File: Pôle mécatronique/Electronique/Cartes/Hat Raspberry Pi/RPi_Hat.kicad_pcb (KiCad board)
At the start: 2 copper layers, 65 x 57.3 mm, 14 parts, among them J1 Conn_02x03_Odd_Even, J2 RPi_GPIO, U1 XBee, U2 MCP25625, Y1 8MHz

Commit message: Update alim correction
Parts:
- added ?: , , F.Cu at (73.4, 67.1)
- added ?: , , F.Cu at (73.4, 62.2)
- added R1: R, Resistor_THT:R_Axial_DIN0207_L6.3mm_D2.5mm_P2.54mm_Vertical, F.Cu at (75.9, 66.5)
- U2: value MCP25625 -> MCP25625-x-SS
- moved R3 22.1 mm to (94.7, 62.0), turned to -90 degrees
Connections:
- J2 pad 39: GND -> unconnected-(J2-Pad39)
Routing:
- net /RPi_GPIO/BCM14_TXD: track 46.4 -> 57.3 mm
- net GND: track 55.7 -> 47.1 mm, vias 6 -> 4
- net 5VRPI: track 79.9 -> 72.4 mm
- net can_L: track 12.3 -> 18.6 mm, vias 2 -> 0
- net 3V3: track 107.8 -> 102.4 mm
- net /RPi_GPIO/BCM15_RXD: track 50.1 -> 53.7 mm
- net cmd_relais: track 33.6 -> 36.6 mm
- net Net-(C3-Pad1): track 22.4 -> 24.5 mm
- net Net-(R3-Pad2): track 7.39 -> 8.38 mm
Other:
- board size 65 x 57.3 mm -> 65 x 58.5 mm

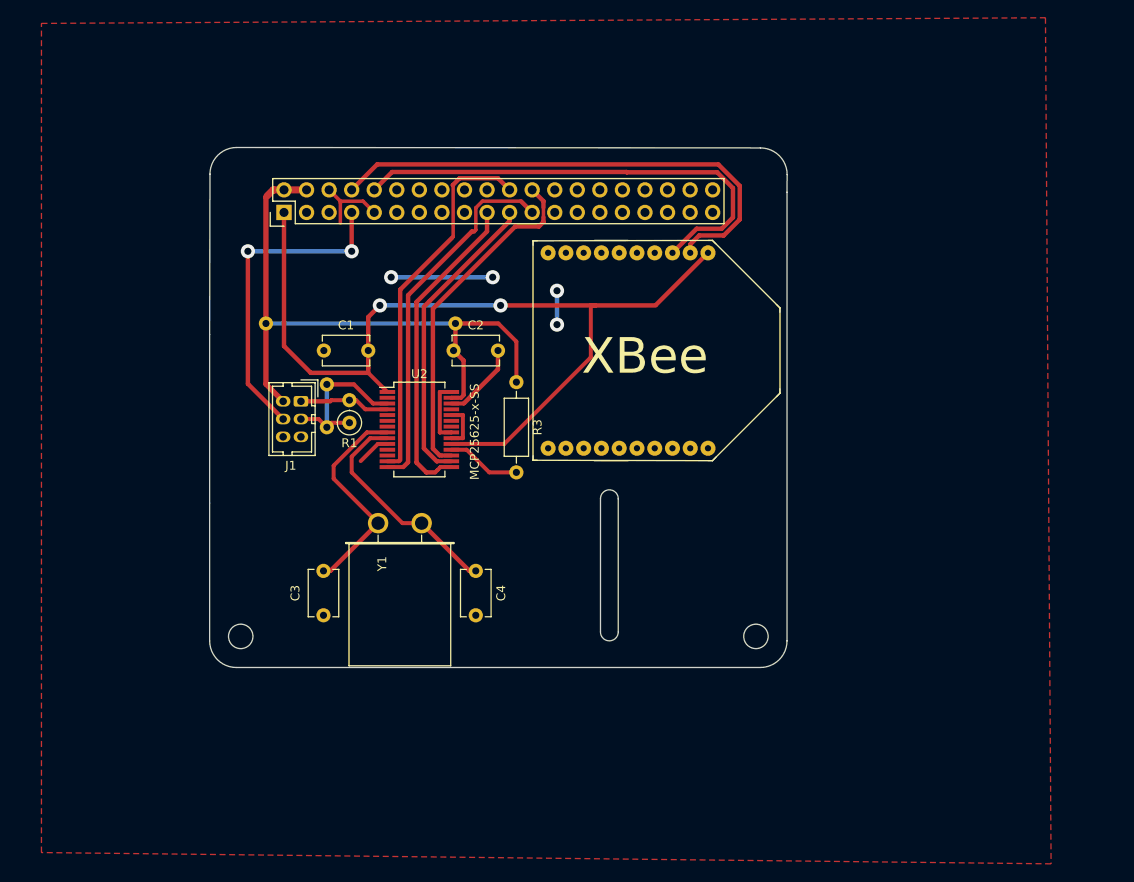
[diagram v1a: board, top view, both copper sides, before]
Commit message: Update HAT
- Ajout des pads
- Correction du schéma
- Corrections diverses
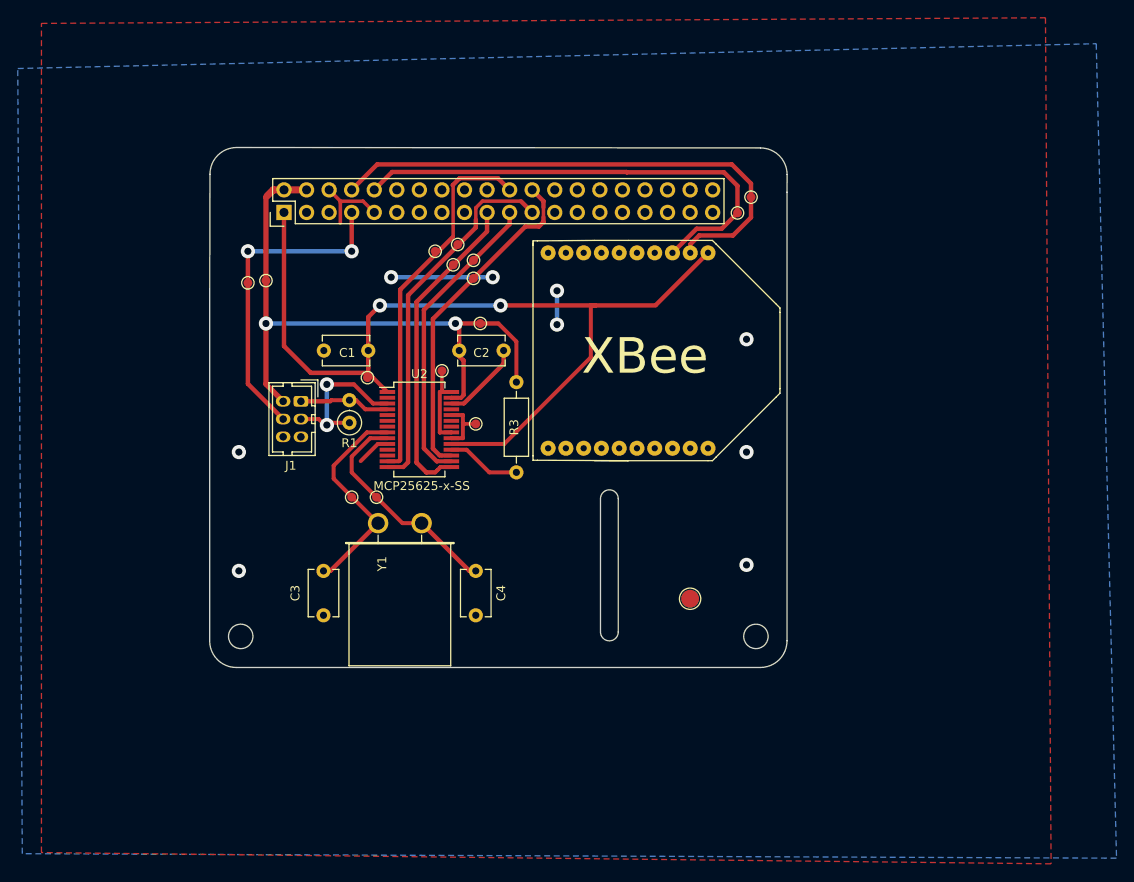
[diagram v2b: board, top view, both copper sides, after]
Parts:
- removed the ? at (73.4, 67.1)
- removed the ? at (66.5, 55.4)
- removed the ? at (73.4, 62.2)
- removed the ? at (87.9, 55.4)
- added  : TestPoint_Pad_D1.0mm, TestPoint:TestPoint_Pad_D1.0mm, F.Cu at (79.0, 74.9)
- added  : TestPoint_Pad_D1.0mm, TestPoint:TestPoint_Pad_D1.0mm, F.Cu at (76.2, 74.9)
- added ?: , , B.Cu at (114.3, 86.4)
- added REF**: TestPoint_Pad_D1.0mm, TestPoint:TestPoint_Pad_D1.0mm, F.Cu at (66.5, 50.5)
- added REF**: TestPoint_Pad_D1.0mm, TestPoint:TestPoint_Pad_D1.0mm, F.Cu at (64.5, 50.8)
- added REF**: TestPoint_Pad_D2.0mm, TestPoint:TestPoint_Pad_D2.0mm, F.Cu at (114.3, 86.4)
- added REF**: TestPoint_Pad_D1.0mm, TestPoint:TestPoint_Pad_D1.0mm, F.Cu at (121.2, 41.1)
- added REF**: TestPoint_Pad_D1.0mm, TestPoint:TestPoint_Pad_D1.0mm, F.Cu at (86.4, 60.7)
- added REF**: TestPoint_Pad_D1.0mm, TestPoint:TestPoint_Pad_D1.0mm, F.Cu at (87.6, 48.8)
- added REF**: TestPoint_Pad_D1.0mm, TestPoint:TestPoint_Pad_D1.0mm, F.Cu at (89.9, 48.3)
- added REF**: TestPoint_Pad_D1.0mm, TestPoint:TestPoint_Pad_D1.0mm, F.Cu at (90.7, 55.4)
- added REF**: TestPoint_Pad_D1.0mm, TestPoint:TestPoint_Pad_D1.0mm, F.Cu at (119.6, 42.9)
- added REF**: TestPoint_Pad_D1.0mm, TestPoint:TestPoint_Pad_D1.0mm, F.Cu at (90.2, 66.7)
- added REF**: TestPoint_Pad_D1.0mm, TestPoint:TestPoint_Pad_D1.0mm, F.Cu at (88.1, 46.5)
- added REF**: TestPoint_Pad_D1.0mm, TestPoint:TestPoint_Pad_D1.0mm, F.Cu at (78.0, 61.5)
- added REF**: TestPoint_Pad_D1.0mm, TestPoint:TestPoint_Pad_D1.0mm, F.Cu at (85.6, 47.2)
- added REF**: TestPoint_Pad_D1.0mm, TestPoint:TestPoint_Pad_D1.0mm, F.Cu at (89.9, 50.3)
- moved C2 0.64 mm to (88.3, 58.4)
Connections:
- net 3V3 renamed +3.3VA
- net 5VRPI renamed +5V
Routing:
- net GND: track 47.1 -> 39.7 mm, vias 4 -> 9
- net /RPi_GPIO/BCM14_TXD: track 57.3 -> 59.9 mm
- net Net-(U2-Pad21): track 7.15 -> 9.36 mm
- net Net-(U2-Pad20): track 5.20 -> 6.72 mm
- net /RPi_GPIO/BCM15_RXD: track 53.7 -> 54.6 mm
- net CS: track 38.8 -> 38.1 mm
- net +5V: track 72.4 -> 72.3 mm, vias 0 -> 2
- net can_L: vias 0 -> 2
- added copper zone on B.Cu, net GND

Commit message: Update
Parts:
- moved J1 2.18 mm to (68.3, 64.0)
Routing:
- net can_H: track 10.2 -> 12.3 mm
- net can_L: track 18.6 -> 20.4 mm
- net +5V: track 72.3 -> 71.4 mm
- net cmd_relais: track 36.6 -> 35.9 mm

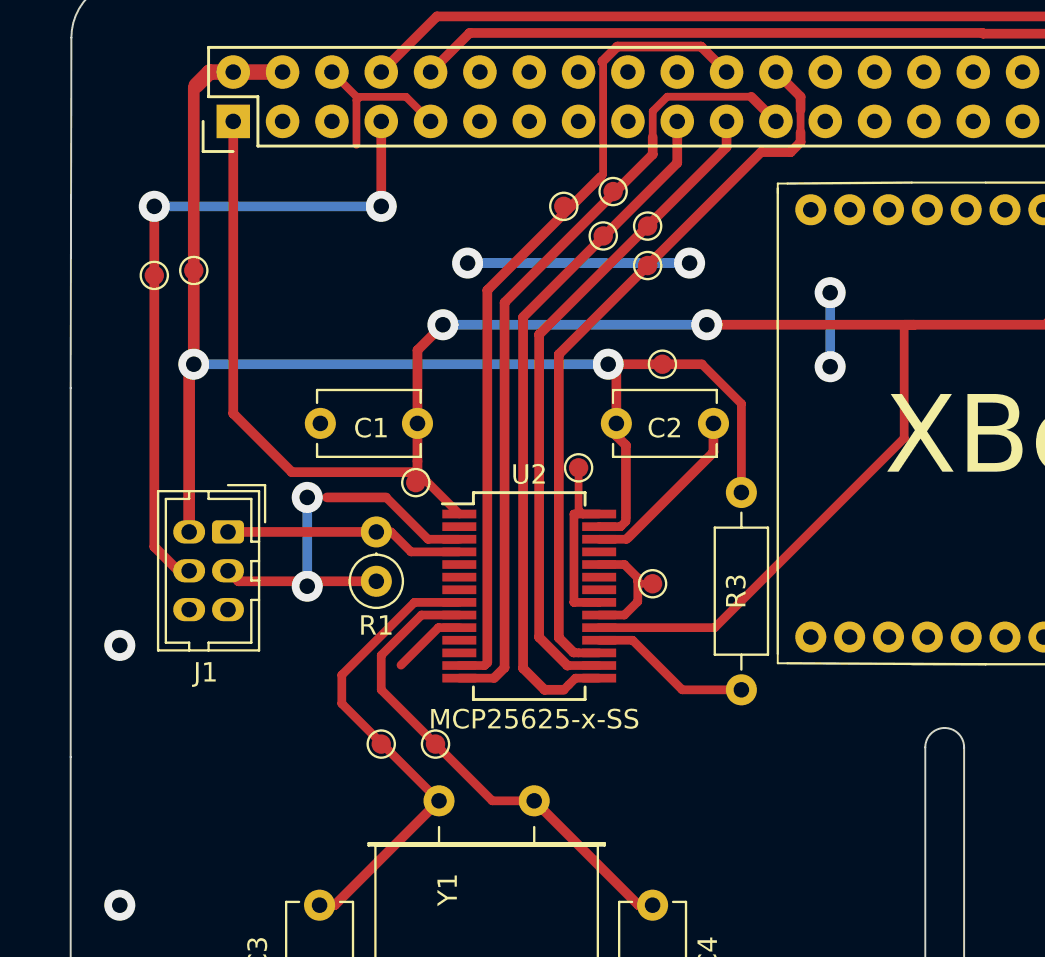
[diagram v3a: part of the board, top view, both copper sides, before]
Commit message: Update HAT & Archi
HAT : - Ajout de l'interrupteur logique de démarrage

Archi : - Update générale
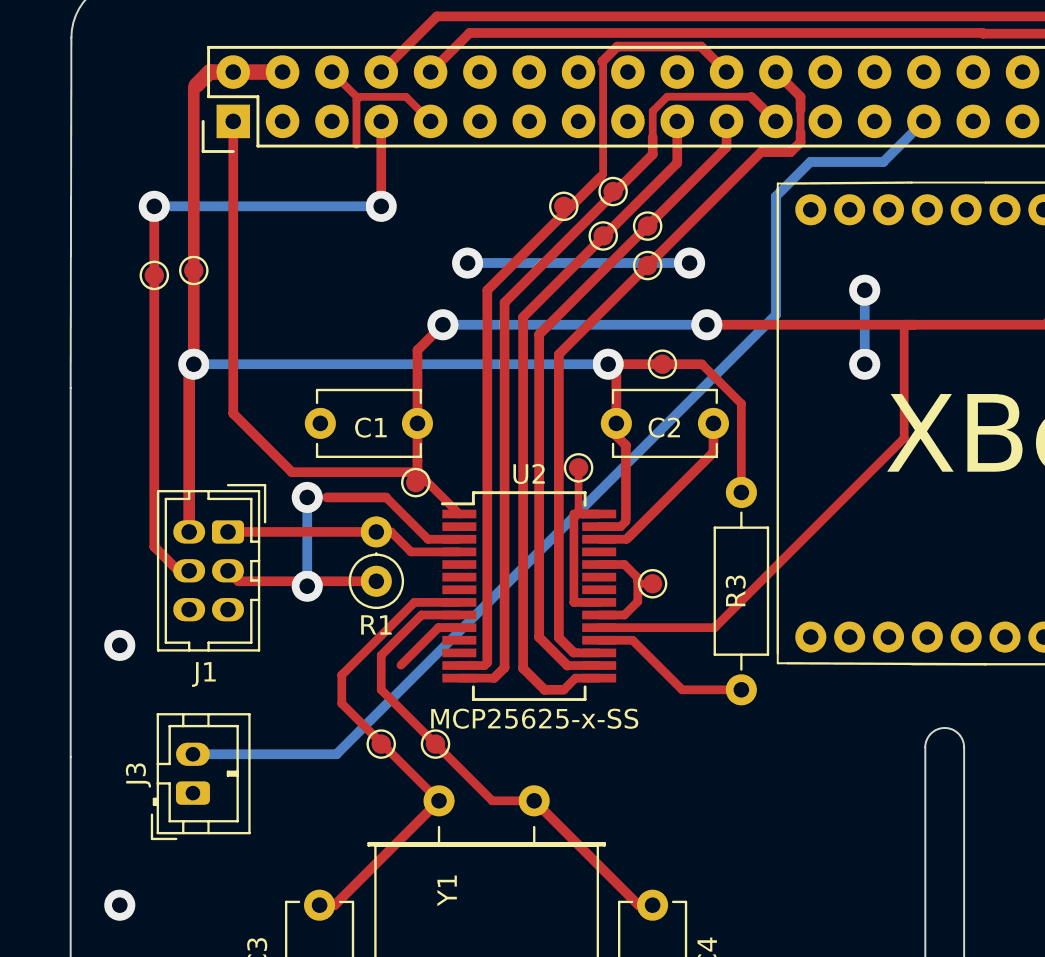
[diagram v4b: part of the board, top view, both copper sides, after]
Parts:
- added J3: Conn_01x02, Connector_JST:JST_PH_B2B-PH-K_1x02_P2.00mm_Vertical, F.Cu at (66.5, 77.5)
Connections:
- J2 pad 29: unconnected-(J2-Pad29) -> /RPi_GPIO/Starter
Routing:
- net /RPi_GPIO/Starter: track 0.00 -> 54.7 mm
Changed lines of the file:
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@@
   (net 22 "unconnected-(J2-Pad27)")
   (net 23 "unconnected-(J2-Pad28)")
-  (net 24 "unconnected-(J2-Pad29)")
+  (net 24 "/RPi_GPIO/Starter")
   (net 25 "unconnected-(J2-Pad31)")
   (net 26 "unconnected-(J2-Pad32)")
@@
       (net 23 "unconnected-(J2-Pad28)") (pinfunction "BCM1_ID_SC") (pintype "bidirectional+no_connect"))
     (pad "29" thru_hole oval locked (at -1.27 11.43 90) (size 1.7272 1.7272) (drill 0.8) (layers *.Cu *.Mask "F.SilkS")
-      (net 24 "unconnected-(J2-Pad29)") (pinfunction "BCM5") (pintype "bidirectional+no_connect"))
+      (net 24 "/RPi_GPIO/Starter") (pinfunction "BCM5") (pintype "bidirectional"))
     (pad "30" thru_hole oval locked (at 1.27 11.43 90) (size 1.7272 1.7272) (drill 0.8) (layers *.Cu *.Mask "F.SilkS")
       (net 66 "unconnected-(J2-Pad30)") (pinfunction "GND") (pintype "power_in+no_connect"))
@@
     )
   )
+  (footprint "Connector_JST:JST_PH_B2B-PH-K_1x02_P2.00mm_Vertical" (layer "F.Cu")
+    (at 66.506 77.454 90)
+    (descr "JST PH series connector, B2B-PH-K (http://www.jst-mfg.com/product/pdf/eng/ePH.pdf), generated with kicad-footprint-generator")
+    (tags "connector JST PH side entry")
+    (property "Sheetfile" "RPi_Hat.kicad_sch")
+    (property "Sheetname" "")
+    (attr through_hole)
+    (fp_text reference "J3" (at 1 -2.9 90) (layer "F.SilkS")
+      (effects (font (size 1 1) (thickness 0.15)))
+    )
+    (fp_text value "Conn_01x02" (at 1 4 90) (layer "F.Fab")
+      (effects (font (size 1 1) (thickness 0.15)))
+    )
+    (fp_text user "${REFERENCE}" (at 1 1.5 90) (layer "F.Fab")
+      (effects (font (size 1 1) (thickness 0.15)))
+    )
+    (fp_line (start -1.45 -1.2) (end -1.45 2.3) (layer "F.SilkS") (width 0.12))
+    (fp_line (start -2.06 -1.81) (end -2.06 2.91) (layer "F.SilkS") (width 0.12))
+    (fp_line (start -2.36 -2.11) (end -2.36 -0.86) (layer "F.SilkS") (width 0.12))
+    (fp_line (start 0.9 2.3) (end 0.9 1.8) (layer "F.SilkS") (width 0.12))
+    (fp_line (start 3.45 2.3) (end 3.45 -1.2) (layer "F.SilkS") (width 0.12))
+    (fp_line (start 0.5 -1.81) (end 0.5 -1.2) (layer "F.SilkS") (width 0.12))
+    (fp_line (start 1 2.3) (end 1 1.8) (layer "F.SilkS") (width 0.12))
+    (fp_line (start 3.45 -1.2) (end 1.5 -1.2) (layer "F.SilkS") (width 0.12))
+    (fp_line (start -2.06 2.91) (end 4.06 2.91) (layer "F.SilkS") (width 0.12))
+    (fp_line (start 1.5 -1.2) (end 1.5 -1.81) (layer "F.SilkS") (width 0.12))
+    (fp_line (start -1.11 -2.11) (end -2.36 -2.11) (layer "F.SilkS") (width 0.12))
+    (fp_line (start -1.45 2.3) (end 3.45 2.3) (layer "F.SilkS") (width 0.12))
+    (fp_line (start 4.06 2.91) (end 4.06 -1.81) (layer "F.SilkS") (width 0.12))
+    (fp_line (start 4.06 -1.81) (end -2.06 -1.81) (layer "F.SilkS") (width 0.12))
+    (fp_line (start 0.9 1.8) (end 1.1 1.8) (layer "F.SilkS") (width 0.12))
+    (fp_line (start -0.3 -1.81) (end -0.3 -2.01) (layer "F.SilkS") (width 0.12))
+    (fp_line (start -2.06 -0.5) (end -1.45 -0.5) (layer "F.SilkS") (width 0.12))
+    (fp_line (start 4.06 0.8) (end 3.45 0.8) (layer "F.SilkS") (width 0.12))
+    (fp_line (start -0.3 -2.01) (end -0.6 -2.01) (layer "F.SilkS") (width 0.12))
+    (fp_line (start 4.06 -0.5) (end 3.45 -0.5) (layer "F.SilkS") (width 0.12))
+    (fp_line (start -0.6 -2.01) (end -0.6 -1.81) (layer "F.SilkS") (width 0.12))
+    (fp_line (start 1.1 1.8) (end 1.1 2.3) (layer "F.SilkS") (width 0.12))
+    (fp_line (start -2.06 0.8) (end -1.45 0.8) (layer "F.SilkS") (width 0.12))
+    (fp_line (start -0.3 -1.91) (end -0.6 -1.91) (layer "F.SilkS") (width 0.12))
+    (fp_line (start 0.5 -1.2) (end -1.45 -1.2) (layer "F.SilkS") (width 0.12))
+    (fp_line (start -2.45 -2.2) (end -2.45 3.3) (layer "F.CrtYd") (width 0.05))
+    (fp_line (start 4.45 -2.2) (end -2.45 -2.2) (layer "F.CrtYd") (width 0.05))
+    (fp_line (start -2.45 3.3) (end 4.45 3.3) (layer "F.CrtYd") (width 0.05))
+    (fp_line (start 4.45 3.3) (end 4.45 -2.2) (layer "F.CrtYd") (width 0.05))
+    (fp_line (start 3.95 -1.7) (end -1.95 -1.7) (layer "F.Fab") (width 0.1))
+    (fp_line (start -1.95 2.8) (end 3.95 2.8) (layer "F.Fab") (width 0.1))
+    (fp_line (start -1.95 -1.7) (end -1.95 2.8) (layer "F.Fab") (width 0.1))
+    (fp_line (start -2.36 -2.11) (end -2.36 -0.86) (layer "F.Fab") (width 0.1))
+    (fp_line (start -1.11 -2.11) (end -2.36 -2.11) (layer "F.Fab") (width 0.1))
+    (fp_line (start 3.95 2.8) (end 3.95 -1.7) (layer "F.Fab") (width 0.1))
+    (pad "1" thru_hole roundrect locked (at 0 0 90) (size 1.2 1.75) (drill 0.75) (layers *.Cu *.Mask) (roundrect_rratio 0.208333)
+      (net 7 "GND") (pinfunction "Pin_1") (pintype "passive"))
+    (pad "2" thru_hole oval locked (at 2 0 90) (size 1.2 1.75) (drill 0.75) (layers *.Cu *.Mask)
+      (net 24 "/RPi_GPIO/Starter") (pinfunction "Pin_2") (pintype "passive"))
+    (model "${KICAD6_3DMODEL_DIR}/Connector_JST.3dshapes/JST_PH_B2B-PH-K_1x02_P2.00mm_Vertical.wrl"
+      (offset (xyz 0 0 0))
+      (scale (xyz 1 1 1))
+      (rotate (xyz 0 0 0))
+    )
+  )
   (footprint "TestPoint:TestPoint_Pad_D1.0mm" (layer "F.Cu")
     (at 119.634 42.926)
@@
   (segment (start 74.923111 41.770667) (end 74.923111 44.075889) (width 0.4) (layer "F.Cu") (net 7))
   (segment (start 88.902975 64.309519) (end 88.827494 64.385) (width 0.45) (layer "F.Cu") (net 7))
-  (via (at 99.314 55.499) (size 1.6) (drill 0.8) (layers "F.Cu" "B.Cu") (free) (net 7))
+  (via (at 101.092 55.372) (size 1.6) (drill 0.8) (layers "F.Cu" "B.Cu") (free) (net 7))
   (via (at 62.738 69.85) (size 1.6) (drill 0.8) (layers "F.Cu" "B.Cu") (free) (net 7))
   (via (at 92.075 50.165) (size 1.6) (drill 0.8) (layers "F.Cu" "B.Cu") (free) (net 7))
@@
   (via (at 62.738 83.225) (size 1.6) (drill 0.8) (layers "F.Cu" "B.Cu") (free) (net 7))
   (via (at 121.666 69.85) (size 1.6) (drill 0.8) (layers "F.Cu" "B.Cu") (free) (net 7))
-  (via (at 99.314 51.689) (size 1.6) (drill 0.8) (layers "F.Cu" "B.Cu") (free) (net 7))
+  (via (at 101.092 51.562) (size 1.6) (drill 0.8) (layers "F.Cu" "B.Cu") (free) (net 7))
   (via (at 121.666 82.55) (size 1.6) (drill 0.8) (layers "F.Cu" "B.Cu") (free) (net 7))
   (via (at 121.666 57.15) (size 1.6) (drill 0.8) (layers "F.Cu" "B.Cu") (free) (net 7))
-  (segment (start 99.314 51.689) (end 99.314 55.499) (width 0.5) (layer "B.Cu") (net 7))
+  (segment (start 101.092 51.562) (end 101.092 55.372) (width 0.5) (layer "B.Cu") (net 7))
   (segment (start 80.645 50.165) (end 92.075 50.165) (width 0.5) (layer "B.Cu") (net 7))
   (segment (start 91.44 45.0088) (end 91.44 42.87) (width 0.5) (layer "F.Cu") (net 15))
@@
   (segment (start 97.79 42.28298) (end 97.79 43.434) (width 0.4) (layer "F.Cu") (net 20))
   (segment (start 95.758 44.45) (end 85.344 54.864) (width 0.5) (layer "F.Cu") (net 20))
+  (segment (start 104.14 42.87) (end 102.052 44.958) (width 0.5) (layer "B.Cu") (net 24))
+  (segment (start 96.52 46.736) (end 96.52 52.832) (width 0.5) (layer "B.Cu") (net 24))
+  (segment (start 102.052 44.958) (end 98.298 44.958) (width 0.5) (layer "B.Cu") (net 24))
+  (segment (start 98.298 44.958) (end 96.52 46.736) (width 0.5) (layer "B.Cu") (net 24))
+  (segment (start 96.52 52.832) (end 73.898 75.454) (width 0.5) (layer "B.Cu") (net 24))
+  (segment (start 73.898 75.454) (end 66.506 75.454) (width 0.5) (layer "B.Cu") (net 24))
   (segment (start 121.158 39.624) (end 121.158 43.434) (width 0.5) (layer "F.Cu") (net 33))
   (segment (start 118.999 37.465) (end 121.158 39.624) (width 0.5) (layer "F.Cu") (net 33))
